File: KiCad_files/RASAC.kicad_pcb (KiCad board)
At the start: 6 copper layers, 147 x 85 mm, 356 parts, among them J1 PCIe_x4_Connector, J12 Conn_01x03, J13 Conn_02x03_Counter_Clockwise, J14 Conn_01x02, J2 PCIe_6_Pin_Power, J3 Conn_01x06, J4 USB_C_Receptacle, J5 TFP410, J6 DB15_Female_HighDensity_Mount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, J7 HDMI_A_1.4, J8 Conn_01x02, J9 Conn_01x02, Q1 Q_NMOS_GSD, Q2 Q_PMOS_GSD, SW1 SW_Push, U1 XC7A35T_CSG325, U10 W25Q128JV, U11 TPD12S521, U12 PCA9306, U13 LM2676-KTW, U2 MAX15027, U3 PI3420, U4 PI3421, U5 PI3420, U6 FT2232HL, U7 93LCxxC, U8 SiT8209, U9 SiT9102, Y1 12MHz

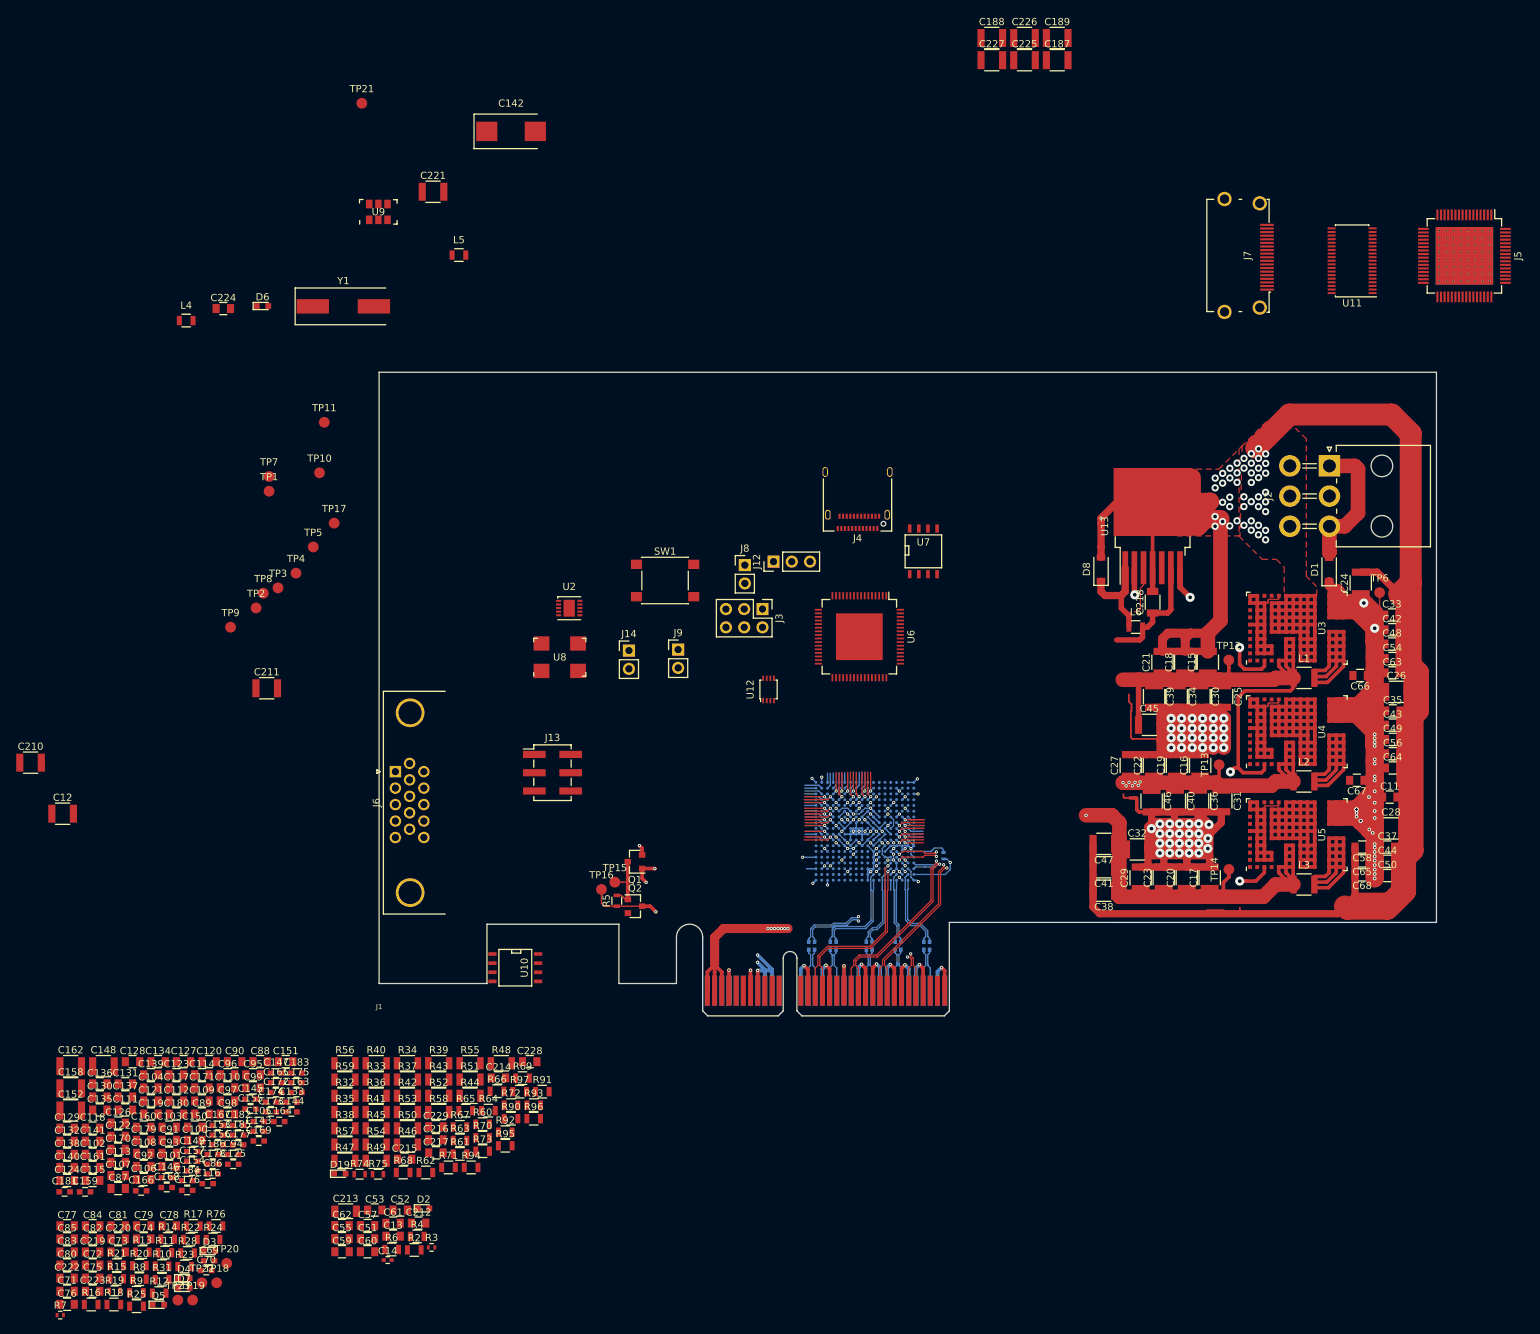
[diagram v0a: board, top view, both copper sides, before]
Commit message: UART + JTAG + half of HDMI
Also resized HDMI resistors from 1206 to 0603
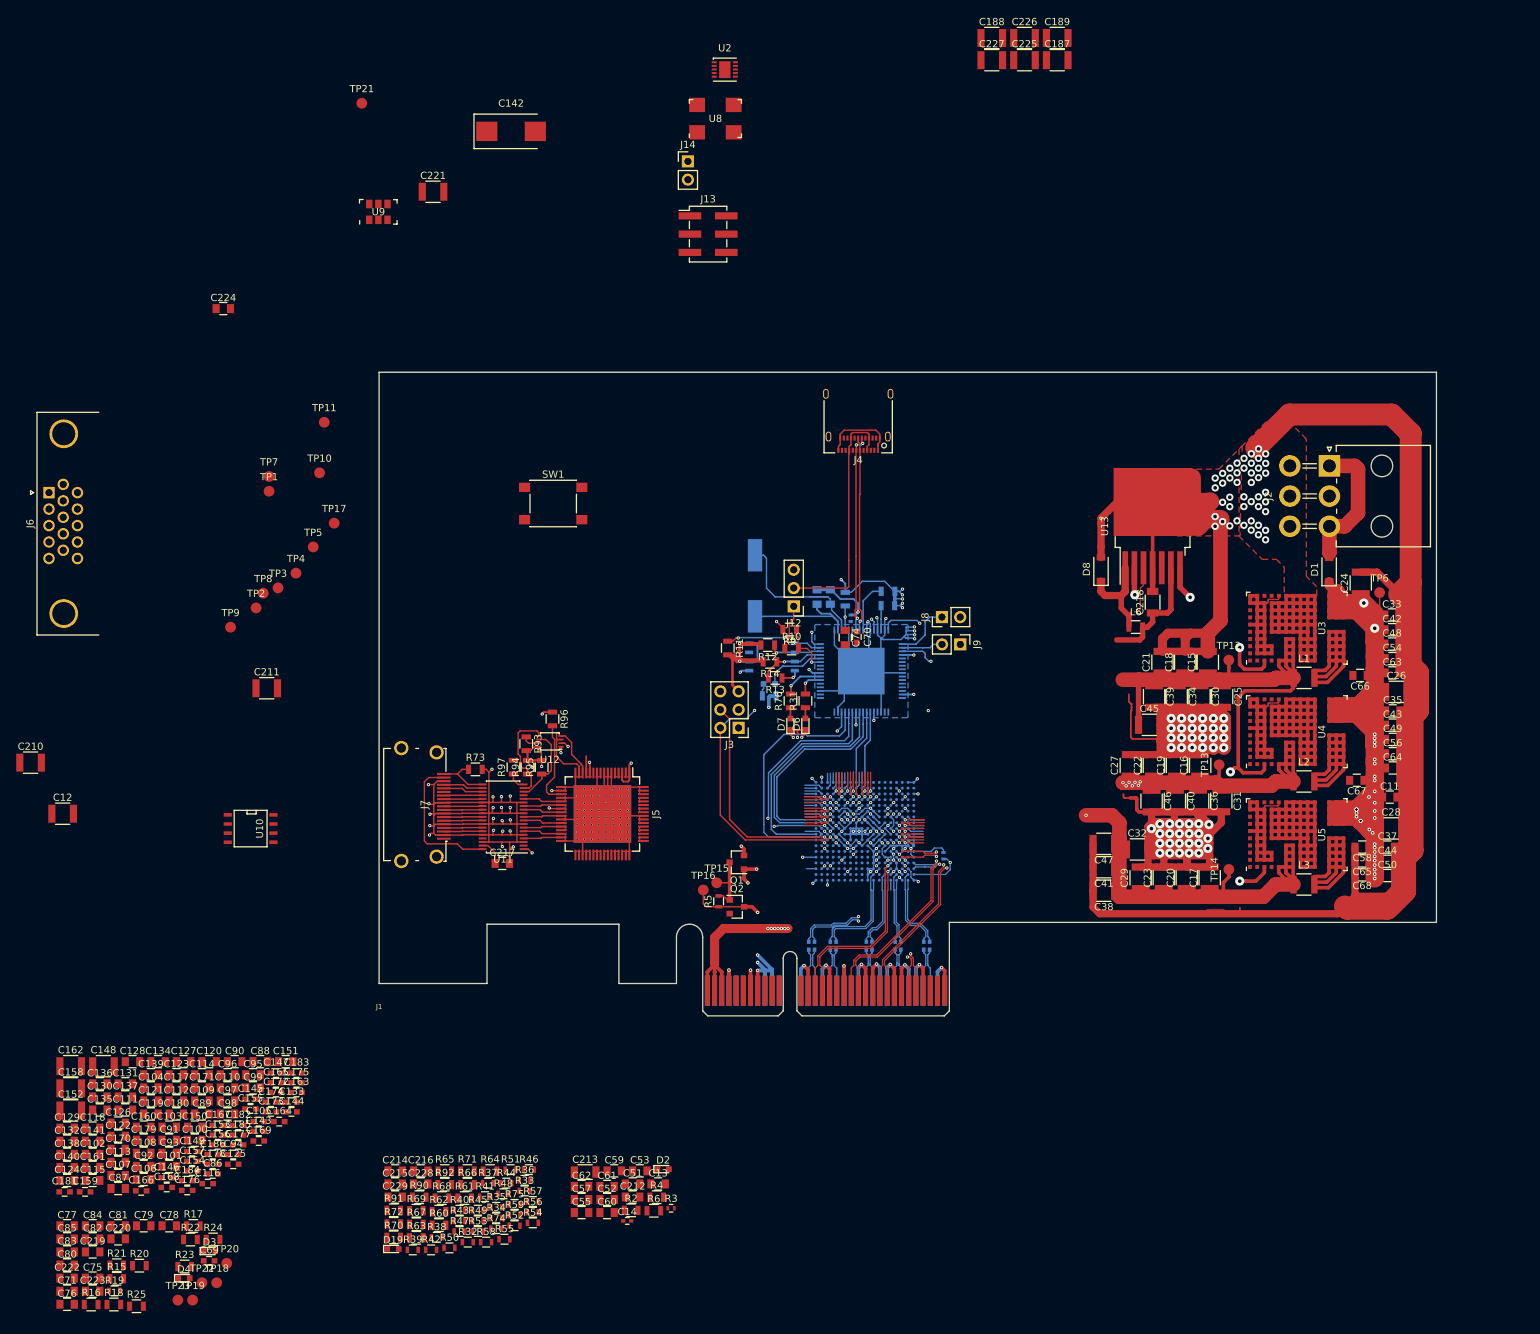
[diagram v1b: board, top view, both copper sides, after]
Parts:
- C72, C73, D5, L4, L5, R28, R7, R8, U6, U7, Y1: moved to B.Cu
- R32, R33, R34, R35, R36, R37, R38, R39, R40, R41, R42, R43, R44, R45, R46, R47, R48, R49, R50, R51, R52, R53, R54, R55, R56, R57, R58, R59: footprint Resistors_SMD:R_1206 -> Resistors_SMD:R_0603
- moved R7 146.5 mm to (147.1, 96.7), turned to 270 degrees
- moved J5 142.8 mm to (112.6, 123.9)
- moved U11 141.1 mm to (98.7, 124.3)
- moved R8 140.0 mm to (152.3, 95.0)
- moved J7 137.6 mm to (84.6, 122.6)
- moved C72 137.0 mm to (142.4, 93.8), turned to 90 degrees
- moved C73 134.5 mm to (144.2, 93.8), turned to 90 degrees
- moved R9 129.4 mm to (138.6, 98.3), turned to 180 degrees
- moved C74 128.5 mm to (146.3, 99.4), turned to 270 degrees
- moved C70 126.3 mm to (147.9, 99.3), turned to 270 degrees
- moved R12 123.6 mm to (135.5, 100.4), turned to 180 degrees
- moved R10 122.6 mm to (138.9, 100.9)
- moved D5 121.1 mm to (135.8, 105.8), turned to 180 degrees
- moved R31 120.3 mm to (140.8, 108.2), turned to 90 degrees
- moved R13 118.8 mm to (136.6, 105.0), turned to 180 degrees
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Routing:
- net VCC3V3: track 12.4 -> 255.0 mm, vias 2 -> 24
- net GND: track 915.8 -> 1130.1 mm, vias 141 -> 175
- net VCC1V8: track 147.6 -> 293.4 mm, vias 25 -> 30
- net JTAG_TDI: track 3.33 -> 71.9 mm
- net JTAG_TMS: track 4.39 -> 71.9 mm, vias 1 -> 4
- net JTAG_TCK: track 5.69 -> 72.1 mm, vias 1 -> 2
- net JTAG_TDO: track 3.36 -> 69.7 mm
- net TTL_DCD1: track 2.47 -> 37.2 mm
- net Net-(J12-Pad2): track 0.00 -> 34.4 mm
- net TTL_DTR1: track 1.54 -> 31.2 mm
- net TTL_DSR1: track 2.46 -> 31.3 mm, vias 0 -> 2
- net TTL_CTS1: track 1.49 -> 29.4 mm
- net USB_DM_1: track 0.00 -> 27.8 mm, vias 0 -> 3
- net TTL_RTS1: track 2.48 -> 29.8 mm
- net USB_DP_1: track 0.00 -> 27.1 mm, vias 0 -> 1
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- added copper zone on B.Cu, net GND

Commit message: More HDMI
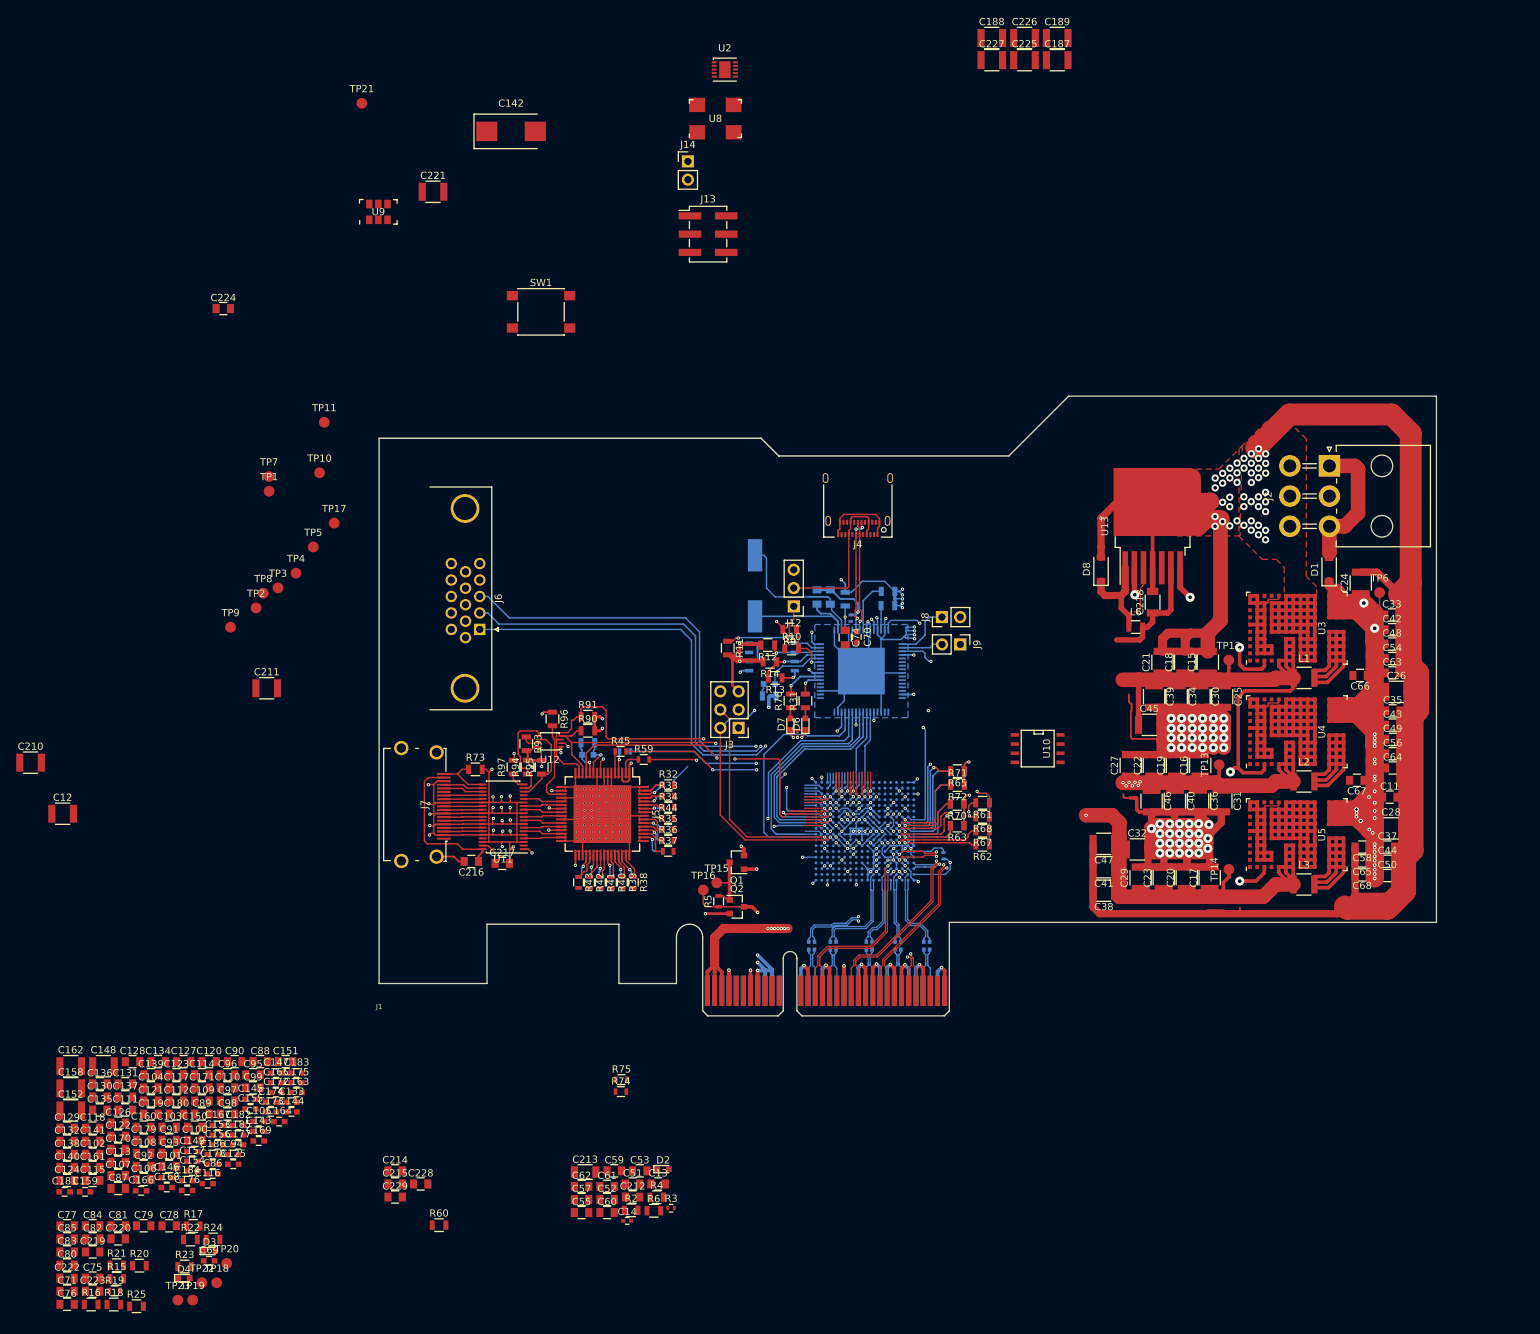
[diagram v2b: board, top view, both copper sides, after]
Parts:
- D19, R46, R47, R48, R49, R50, R51, R52, R53, R54, R55, R56, R57, R58, R64, R66, R69, R71, R92: moved to B.Cu
- moved U10 110.0 mm to (173.1, 114.8)
- moved R72 99.3 mm to (161.9, 119.9), turned to 180 degrees
- moved R70 98.8 mm to (161.9, 122.5), turned to 180 degrees
- moved R67 95.9 mm to (165.4, 126.3), turned to 180 degrees
- moved R63 94.6 mm to (161.9, 125.5), turned to 180 degrees
- moved R69 92.3 mm to (161.9, 125.5), turned to 180 degrees
- moved R68 92.0 mm to (165.4, 124.3), turned to 180 degrees
- moved R62 91.2 mm to (165.4, 128.2), turned to 180 degrees
- moved R61 90.6 mm to (165.4, 122.4), turned to 180 degrees
- moved R65 90.4 mm to (161.9, 118.0), turned to 180 degrees
- moved R66 89.2 mm to (161.9, 118.0), turned to 180 degrees
- moved R71 86.8 mm to (161.9, 119.9), turned to 180 degrees
- moved R64 82.6 mm to (161.9, 122.5), turned to 180 degrees
- moved D19 73.9 mm to (110.5, 115.7), turned to 180 degrees
- moved R91 73.8 mm to (110.5, 110.4)
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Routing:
- net Net-(J6-Pad2): track 0.00 -> 100.7 mm, vias 0 -> 2
- net Net-(J6-Pad1): track 0.00 -> 99.4 mm, vias 0 -> 2
- net VCC3V3: track 255.0 -> 352.9 mm, vias 24 -> 29
- net Net-(J6-Pad3): track 0.00 -> 93.5 mm, vias 0 -> 2
- net HDMI_SCL: track 11.1 -> 83.3 mm, vias 0 -> 2
- net HDMI_SDA: track 9.94 -> 78.4 mm, vias 1 -> 2
- net HDMI_RST: track 4.85 -> 44.3 mm, vias 0 -> 2
- net HDMI_R_HSYNC: track 1.54 -> 34.5 mm, vias 0 -> 2
- net HDMI_R_VSYNC: track 1.53 -> 31.8 mm, vias 0 -> 3
- net HDMI_R_DE: track 3.34 -> 33.1 mm, vias 1 -> 3
- net HPD: track 0.00 -> 16.0 mm, vias 0 -> 2
- net GND: track 1130.1 -> 1146.1 mm, vias 175 -> 177
- net Net-(J12-Pad2): track 34.4 -> 22.4 mm
- net USB_DP_1: track 27.1 -> 15.4 mm
- net USB_DM_1: track 27.8 -> 16.1 mm
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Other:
- board size 147 x 85 mm -> 147 x 81.7 mm

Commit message: Some more HDMI + power
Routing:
- net HDMI_R_D15: track 2.24 -> 51.8 mm, vias 0 -> 2
- net HDMI_R_D12: track 2.32 -> 50.9 mm, vias 0 -> 2
- net HDMI_R_D14: track 1.28 -> 48.8 mm, vias 0 -> 2
- net HDMI_R_D13: track 1.31 -> 48.7 mm, vias 0 -> 2
- net HDMI_R_D2: track 2.37 -> 33.7 mm, vias 0 -> 2
- net HDMI_R_D3: track 1.34 -> 32.0 mm, vias 0 -> 2
- net VCC3V3: track 352.9 -> 382.8 mm, vias 29 -> 39
- net HDMI_R_D0: track 4.91 -> 34.2 mm, vias 1 -> 2
- net HDMI_R_D4: track 1.34 -> 30.5 mm, vias 0 -> 2
- net HDMI_R_D6: track 3.16 -> 29.3 mm, vias 1 -> 2
- net HDMI_R_D1: track 6.54 -> 32.2 mm, vias 1 -> 2
- net HDMI_R_D11: track 3.17 -> 28.5 mm, vias 1 -> 3
- net HDMI_R_D5: track 4.06 -> 28.3 mm, vias 1 -> 2
- net HDMI_R_D10: track 3.37 -> 27.3 mm, vias 1 -> 2
- net HDMI_R_D9: track 3.36 -> 27.3 mm, vias 1 -> 2
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
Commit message: HDMI Done?
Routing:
- net HDMI_R_D20: track 1.59 -> 51.3 mm, vias 0 -> 3
- net HDMI_R_D16: track 2.52 -> 50.4 mm, vias 0 -> 2
- net HDMI_R_D18: track 2.50 -> 48.5 mm, vias 0 -> 2
- net HDMI_R_D19: track 1.60 -> 46.7 mm, vias 0 -> 2
- net HDMI_R_D17: track 2.55 -> 47.5 mm, vias 0 -> 2
- net HDMI_R_D22: track 3.38 -> 45.6 mm, vias 1 -> 2
- net HDMI_R_D21: track 6.43 -> 47.8 mm, vias 1 -> 2
- net HDMI_R_D23: track 9.14 -> 44.0 mm, vias 2 -> 3
- net VCC3V3: track 382.8 -> 386.2 mm, vias 39 -> 40

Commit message: Almost done
Just gotta do capacitors, I think
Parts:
- C12, C210, C211, R60, SW1, U9: moved to B.Cu
- moved C210 164.0 mm to (195.7, 95.7), turned to 270 degrees
- moved C12 154.5 mm to (189.4, 95.7), turned to 270 degrees
- moved R21 149.6 mm to (174.8, 112.3), turned to 270 degrees
- moved C222 149.1 mm to (176.3, 132.5)
- moved C71 148.9 mm to (152.4, 94.8)
- moved R20 148.7 mm to (174.8, 108.9), turned to 270 degrees
- moved C83 148.5 mm to (176.3, 130.4)
- moved R16 146.5 mm to (162.9, 110.2)
- moved TP22 143.0 mm to (173.3, 106.1)
- moved R18 141.7 mm to (162.9, 114.1)
- moved R22 133.5 mm to (170.1, 115.0), turned to 180 degrees
- moved C69 132.5 mm to (152.2, 93.0)
- moved TP18 132.1 mm to (161.7, 106.1)
- moved TP20 129.8 mm to (176.2, 127.8)
- moved R17 127.6 mm to (162.9, 112.1)
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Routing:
- net VCC5V0: track 42.6 -> 212.6 mm, vias 3 -> 11
- net GND: track 1169.7 -> 1315.7 mm, vias 184 -> 213
- net MGTAVCC: track 123.0 -> 248.7 mm, vias 11 -> 26
- net VCC1V8: track 289.8 -> 411.4 mm, vias 29 -> 44
- net VCC3V3: track 386.2 -> 498.8 mm, vias 40 -> 50
- net VGA_HS: track 2.41 -> 57.9 mm, vias 0 -> 3
- net VGA_VS: track 4.96 -> 60.2 mm, vias 1 -> 2
- net PCIe_PRSNT_B: track 0.00 -> 43.1 mm, vias 0 -> 2
- net EMCCLK: track 1.42 -> 40.4 mm, vias 0 -> 2
- net PCIe_PERST: track 4.19 -> 37.6 mm, vias 1 -> 2
- net PCIe_WAKE_B: track 4.95 -> 36.7 mm, vias 1 -> 2
- net VCC2V5: track 0.00 -> 31.3 mm, vias 0 -> 2
- net Net-(J13-Pad2): track 4.23 -> 35.4 mm, vias 1 -> 2
- net SYSCLK_P: track 3.20 -> 32.3 mm, vias 1 -> 2
- net D03: track 3.19 -> 31.2 mm
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
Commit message: Am...  Am I done...?
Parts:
- C100, C102, C103, C105, C108, C109, C110, C111, C112, C113, C114, C116, C119, C120, C121, C122, C123, C125, C127, C128, C129, C130, C131, C132, C135, C136, C137, C138, C139, C140, C145, C148, C150, C151, C155, C159, C160, C161, C167, C170, C171, C179, C180, C181, C212, C219, C75, C80, C84, C85, C87, C88, C89, C90, C91, C92, C94, C97, C98, C99, D3, D4, R15, R23, R24, R25, TP23: moved to B.Cu
- moved C140 168.1 mm to (177.1, 78.6)
- moved C138 164.0 mm to (173.5, 78.7), turned to 180 degrees
- moved C87 162.0 mm to (177.0, 81.8), turned to 90 degrees
- moved C161 161.6 mm to (175.1, 81.8), turned to 90 degrees
- moved C102 159.0 mm to (173.1, 81.8), turned to 90 degrees
- moved C132 159.0 mm to (173.1, 85.5), turned to 270 degrees
- moved C129 156.3 mm to (171.1, 85.5), turned to 270 degrees
- moved C103 155.5 mm to (177.1, 74.8)
- moved C91 155.4 mm to (177.1, 76.7)
- moved C122 154.2 mm to (175.1, 85.5), turned to 270 degrees
- moved C176 154.2 mm to (177.9, 83.4), turned to 90 degrees
- moved C170 154.0 mm to (171.1, 81.8), turned to 90 degrees
- moved C113 153.5 mm to (169.2, 81.8), turned to 90 degrees
- moved C160 152.2 mm to (177.0, 85.5), turned to 270 degrees
- moved R19 150.7 mm to (170.2, 106.8)
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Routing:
- net GND: track 1315.7 -> 1847.8 mm, vias 213 -> 295
- net MGTAVCC: track 248.7 -> 549.7 mm, vias 26 -> 32
- net VCC1V8: track 411.4 -> 485.9 mm, vias 44 -> 47
- net MGTAVTT: track 111.3 -> 184.4 mm, vias 6 -> 7
- net VCC3V3: track 498.8 -> 553.0 mm, vias 50 -> 54
- net Net-(D3-Pad2): track 3.33 -> 18.9 mm, vias 1 -> 2
- net PCIe_12V: track 315.3 -> 329.3 mm, vias 46 -> 47
- net Net-(D4-Pad2): track 0.57 -> 9.49 mm, vias 1 -> 2
- net Net-(J7-Pad1): track 0.00 -> 5.42 mm
- net SYSCLK_N: track 30.9 -> 35.2 mm
- net Net-(R25-Pad2): track 24.5 -> 27.8 mm
- net SYSCLK_P: track 32.3 -> 34.5 mm
- net FCS_B: track 28.4 -> 30.1 mm, vias 1 -> 2
- net EMCCLK: track 40.4 -> 42.0 mm
- net Net-(D2-Pad2): track 0.00 -> 1.40 mm
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
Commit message: Added text + logo + output files
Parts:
- added REF***: OSHW-Logo_11.4x12mm_SilkScreen, Symbols:OSHW-Logo_11.4x12mm_SilkScreen, F.Cu at (104.8, 86.9)
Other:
- board text added: "RASAC Rev 0.9 Brian Hong Jasmine Tang"
